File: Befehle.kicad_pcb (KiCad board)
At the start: 2 copper layers, 100 x 160 mm, 23 parts, among them P1 CONN_01X07, P2 CONN_01X07, U2 74LS540, U3 74LS541, U5 74LS373, U8 74LS139

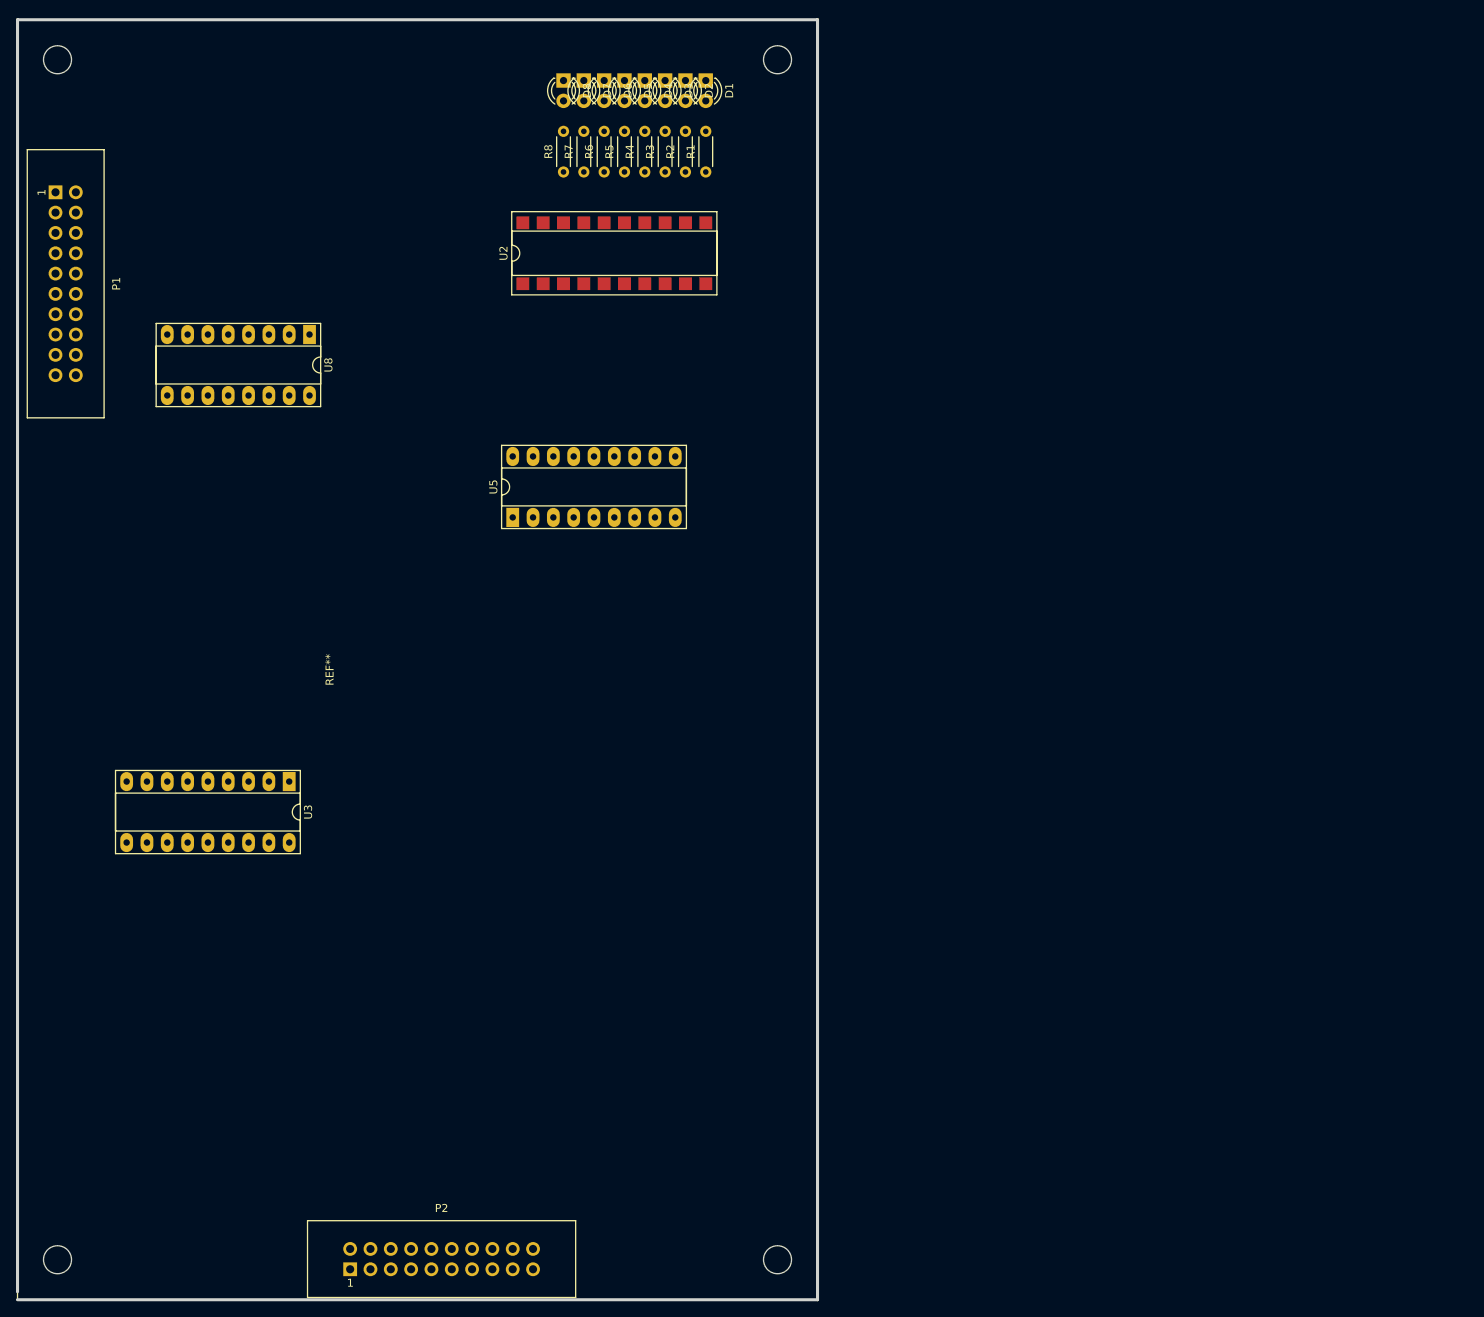
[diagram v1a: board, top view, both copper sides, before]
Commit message: Befehle Footprints und Leiterbahnen added
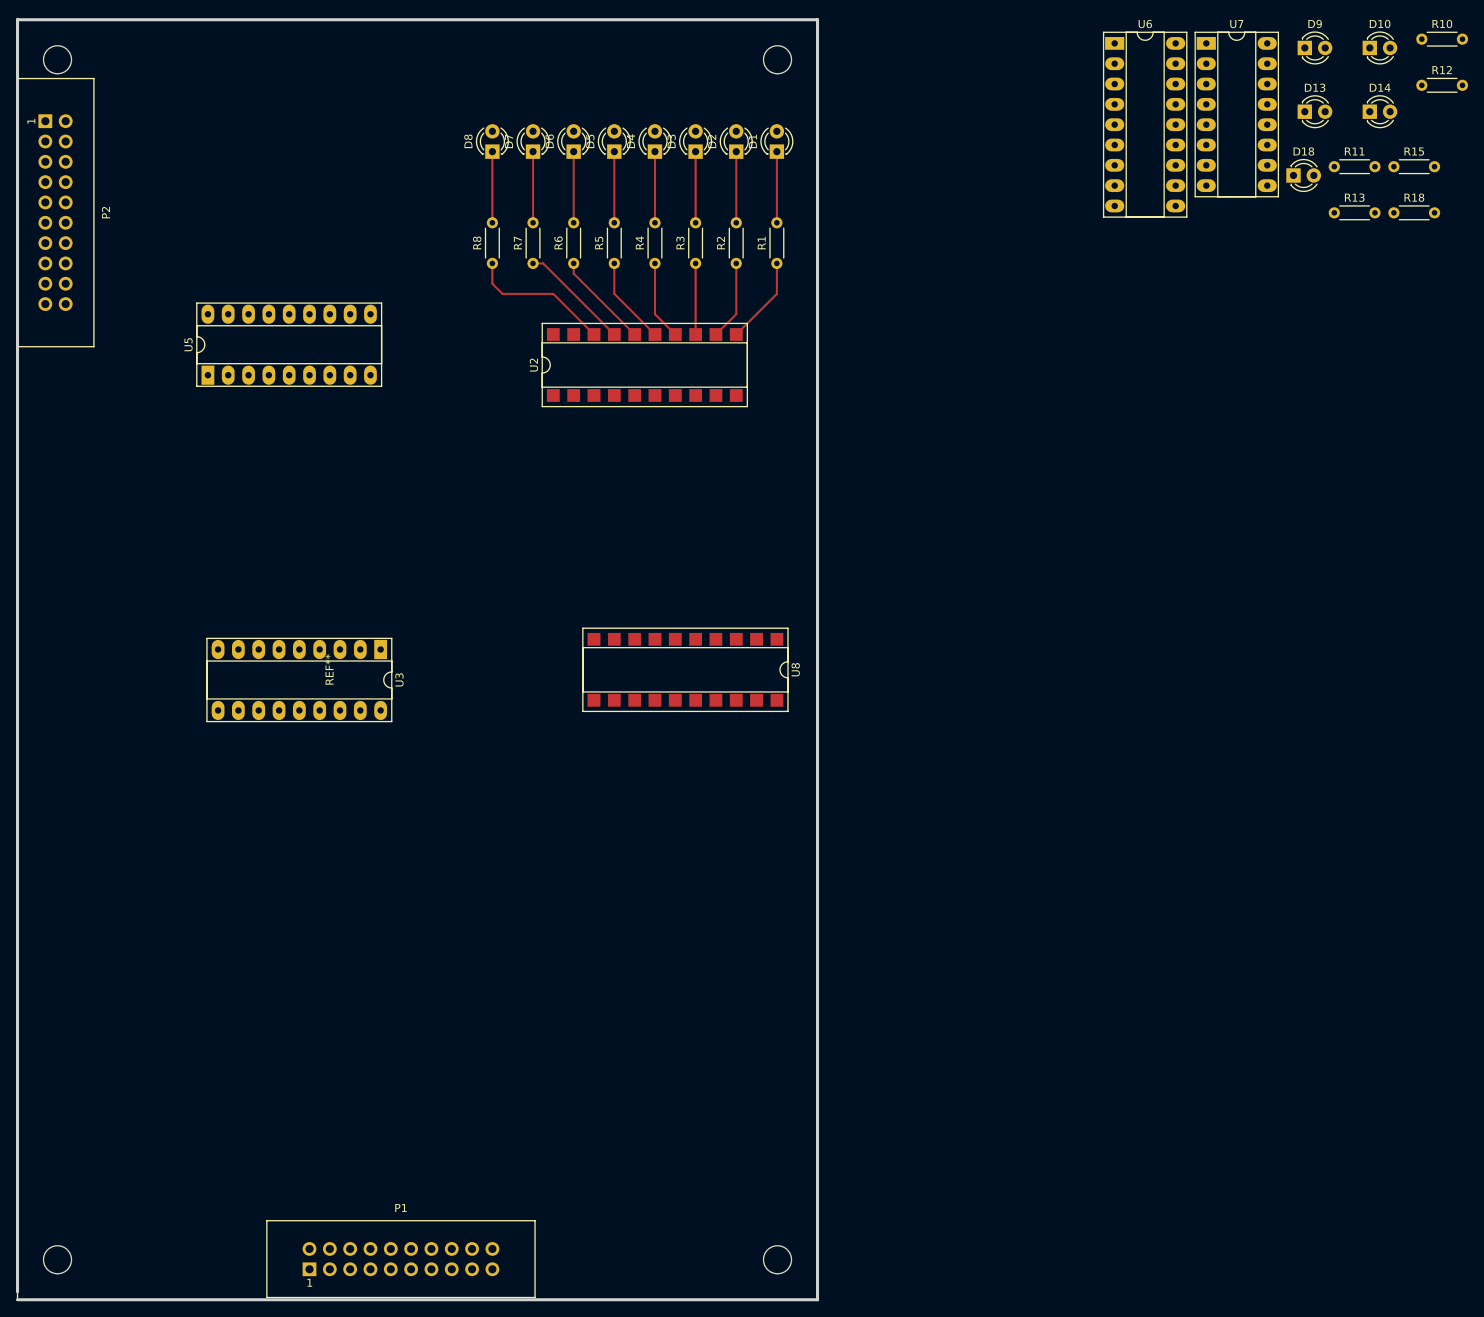
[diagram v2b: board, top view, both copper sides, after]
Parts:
- added D10: Led_Small, LEDs:LED_D3.0mm, F.Cu at (189.7, 21.3)
- added D13: Led_Small, LEDs:LED_D3.0mm, F.Cu at (181.6, 29.3)
- added D14: Led_Small, LEDs:LED_D3.0mm, F.Cu at (189.7, 29.3)
- added D18: LED, LEDs:LED_D3.0mm, F.Cu at (180.1, 37.3)
- added D9: Led_Small, LEDs:LED_D3.0mm, F.Cu at (181.6, 21.3)
- added R10: 330, Resistors_ThroughHole:R_Axial_DIN0204_L3.6mm_D1.6mm_P5.08mm_Horizontal, F.Cu at (196.2, 20.2)
- added R11: 330, Resistors_ThroughHole:R_Axial_DIN0204_L3.6mm_D1.6mm_P5.08mm_Horizontal, F.Cu at (185.2, 36.2)
- added R12: 330, Resistors_ThroughHole:R_Axial_DIN0204_L3.6mm_D1.6mm_P5.08mm_Horizontal, F.Cu at (196.2, 26.0)
- added R13: 330, Resistors_ThroughHole:R_Axial_DIN0204_L3.6mm_D1.6mm_P5.08mm_Horizontal, F.Cu at (185.2, 41.9)
- added R15: 330, Resistors_ThroughHole:R_Axial_DIN0204_L3.6mm_D1.6mm_P5.08mm_Horizontal, F.Cu at (192.7, 36.2)
- added R18: 330, Resistors_ThroughHole:R_Axial_DIN0204_L3.6mm_D1.6mm_P5.08mm_Horizontal, F.Cu at (192.7, 41.9)
- added U6: 74LS373, Housings_DIP:DIP-18_W7.62mm_Socket_LongPads, F.Cu at (157.8, 20.8)
- added U7: 74LS139, Housings_DIP:DIP-16_W7.62mm_Socket_LongPads, F.Cu at (169.2, 20.8)
- D3, D4, D7: value Led_Small -> LED
- P2: value CONN_01X07 -> CONN_02X10
- R1: value 330 -> 4,7k
- R4: value 330 -> 1k
- U2: value 74LS540 -> 74LS04
- U3: value 74LS541 -> 7400
- U5: value 74LS373 -> 74LS541
- U8: value 74LS139 -> 74LS540; footprint Housings_DIP:DIP-16_W7.62mm_Socket_LongPads -> Housings_DIP:DIP-20_W7.62mm_SMDSocket_SmallPads
- moved P2 148.5 mm to (24.1, 30.5), turned to 270 degrees
- moved P1 138.3 mm to (57.1, 174.0), turned to 0 degrees
- moved U8 63.0 mm to (104.1, 99.1)
- moved U5 42.0 mm to (44.5, 62.2)
- moved U3 20.1 mm to (66.0, 96.5)
- moved R8 14.5 mm to (80.0, 48.3)
- moved U2 14.5 mm to (99.1, 61.0)
- moved R1 14.5 mm to (115.6, 48.3)
- moved R2 13.1 mm to (110.5, 48.3)
- moved R7 13.1 mm to (85.1, 48.3)
- moved D8 12.6 mm to (80.0, 34.3), turned to 90 degrees
- moved D1 12.6 mm to (115.6, 34.3), turned to 90 degrees
- moved R3 12.0 mm to (105.4, 48.3)
- moved R6 12.0 mm to (90.2, 48.3)
- moved R4 11.5 mm to (100.3, 48.3)
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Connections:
- D1 pad 2: Net-(D1-Pad2) -> VCC
- D2 pad 2: Net-(D2-Pad2) -> VCC
- D4 pad 2: Net-(D4-Pad2) -> VCC
- D7 pad 2: Net-(D7-Pad2) -> VCC
- P2 pad 10: (no net) -> Net-(P2-Pad10)
- P2 pad 11: (no net) -> Net-(P2-Pad11)
- P2 pad 12: (no net) -> Net-(P2-Pad12)
- P2 pad 13: (no net) -> Net-(P2-Pad13)
- P2 pad 14: (no net) -> Net-(P2-Pad14)
- P2 pad 15: (no net) -> Net-(P2-Pad15)
- P2 pad 16: (no net) -> Net-(P2-Pad16)
- P2 pad 17: (no net) -> Net-(P2-Pad17)
- P2 pad 18: (no net) -> Net-(P2-Pad18)
- P2 pad 19: (no net) -> Net-(P2-Pad19)
- P2 pad 20: (no net) -> Net-(P2-Pad20)
- P2 pad 8: (no net) -> Net-(P2-Pad8)
- P2 pad 9: (no net) -> Net-(P2-Pad9)
- R1 pad 1: Net-(R1-Pad1) -> VCC
- R1 pad 2: Net-(D1-Pad1) -> enableR
- R2 pad 1: Net-(R2-Pad1) -> Net-(D1-Pad1)
- R2 pad 2: Net-(D2-Pad1) -> Net-(R2-Pad2)
- R3 pad 1: Net-(R3-Pad1) -> Net-(D2-Pad1)
- R3 pad 2: Net-(D3-Pad1) -> Net-(R3-Pad2)
- R4 pad 2: Net-(D4-Pad1) -> VCC
- R5 pad 2: Net-(D5-Pad1) -> Net-(R5-Pad2)
- R6 pad 1: Net-(R6-Pad1) -> Net-(D4-Pad1)
- R6 pad 2: Net-(D6-Pad1) -> Net-(R6-Pad2)
- R7 pad 2: Net-(D7-Pad1) -> Net-(D5-Pad1)
- R8 pad 2: Net-(D8-Pad1) -> Net-(D6-Pad1)
- U2 pad 1: Net-(U2-Pad1) -> Net-(R4-Pad1)
- U2 pad 10: GND -> Net-(R17-Pad2)
- U2 pad 11: Net-(R1-Pad1) -> 1
- U2 pad 12: Net-(R2-Pad1) -> Net-(R21-Pad2)
- U2 pad 13: Net-(R3-Pad1) -> 0
- U2 pad 14: Net-(R4-Pad1) -> VCC
- U2 pad 15: Net-(R5-Pad1) -> (no net)
- U2 pad 16: Net-(R6-Pad1) -> (no net)
- U2 pad 17: Net-(R7-Pad1) -> (no net)
- U2 pad 18: Net-(R8-Pad1) -> (no net)
- U2 pad 19: Net-(U2-Pad1) -> (no net)
- U2 pad 2: /a8 -> Net-(R2-Pad2)
- U2 pad 20: VCC -> (no net)
- U2 pad 3: /a7 -> loadIR
- U2 pad 4: /a6 -> Net-(R5-Pad2)
- U2 pad 5: /a5 -> 3
- U2 pad 6: /a4 -> Net-(R6-Pad2)
- U2 pad 7: /a3 -> GND
- U2 pad 8: /a2 -> Net-(R9-Pad2)
- U2 pad 9: /a1 -> 2
- U3 pad 1: Net-(U1-Pad2) -> incPCz
- U3 pad 10: GND -> Net-(U3-Pad10)
- U3 pad 11: Net-(U3-Pad11) -> upPC
- U3 pad 13: Net-(U3-Pad13) -> Net-(U3-Pad12)
- U3 pad 14: Net-(U3-Pad14) -> VCC
- U3 pad 15: Net-(U3-Pad15) -> (no net)
- U3 pad 16: Net-(U3-Pad16) -> (no net)
- U3 pad 17: Net-(U3-Pad17) -> (no net)
- U3 pad 18: Net-(U3-Pad11) -> (no net)
- U3 pad 2: /a8 -> incPCz
- U3 pad 3: /a7 -> Net-(U3-Pad3)
- U3 pad 4: /a6 -> Net-(R4-Pad1)
- U3 pad 5: /a5 -> Net-(U3-Pad3)
- U3 pad 6: /a4 -> Net-(U3-Pad10)
- U3 pad 7: /a3 -> GND
- U3 pad 8: GND -> Net-(U3-Pad8)
- U3 pad 9: GND -> incPC
- U5 pad 1: VCC -> Net-(U1-Pad6)
- U5 pad 11: Net-(R11-Pad2) -> Net-(P2-Pad3)
- U5 pad 12: /a4 -> Net-(P2-Pad5)
- U5 pad 13: Net-(U5-Pad13) -> Net-(P2-Pad7)
- U5 pad 14: Net-(U5-Pad14) -> Net-(P2-Pad9)
- U5 pad 15: /a3 -> Net-(P2-Pad11)
- U5 pad 16: Net-(U5-Pad16) -> Net-(P2-Pad13)
- U5 pad 17: Net-(U5-Pad17) -> Net-(P2-Pad15)
- U5 pad 18: Net-(U5-Pad18) -> Net-(P2-Pad17)
- U5 pad 3: Net-(U5-Pad3) -> /a7
- U5 pad 4: Net-(U5-Pad4) -> /a6
- U5 pad 5: /a7 -> /a5
- U5 pad 6: /a6 -> /a4
- U5 pad 7: Net-(U5-Pad7) -> /a3
- U5 pad 8: Net-(U5-Pad8) -> GND
- U5 pad 9: /a5 -> GND
- U8 pad 1: GND -> Net-(U8-Pad1)
- U8 pad 10: (no net) -> GND
- U8 pad 11: (no net) -> Net-(R18-Pad1)
- U8 pad 12: (no net) -> Net-(R15-Pad1)
- U8 pad 13: (no net) -> Net-(R13-Pad1)
- U8 pad 14: (no net) -> Net-(R12-Pad1)
- U8 pad 15: (no net) -> Net-(R11-Pad1)
- U8 pad 16: VCC -> Net-(R10-Pad1)
- U8 pad 2: Net-(U5-Pad19) -> /a8
- U8 pad 3: Net-(U5-Pad16) -> /a7
- U8 pad 4: Net-(U8-Pad4) -> /a6
- U8 pad 5: Net-(U8-Pad5) -> /a5
- U8 pad 6: Net-(U8-Pad6) -> /a4
- U8 pad 7: Net-(U8-Pad7) -> /a3
- U8 pad 8: GND -> /a2
- U8 pad 9: (no net) -> /a1
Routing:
- net Net-(D4-Pad1): track 0.00 -> 20.9 mm
- net Net-(R8-Pad1): track 0.00 -> 17.9 mm
- net Net-(D2-Pad1): track 0.00 -> 17.8 mm
- net Net-(D1-Pad1): track 0.00 -> 15.2 mm
- net Net-(R7-Pad1): track 0.00 -> 13.8 mm
- net Net-(R5-Pad1): track 0.00 -> 11.0 mm
- net Net-(D8-Pad1): track 0.00 -> 8.89 mm
- net Net-(D7-Pad1): track 0.00 -> 8.89 mm
- net Net-(D6-Pad1): track 0.00 -> 8.89 mm
- net Net-(D5-Pad1): track 0.00 -> 8.89 mm
- net Net-(D3-Pad1): track 0.00 -> 8.89 mm
- net VCC: track 0.00 -> 7.40 mm
- net 1: track 0.00 -> 7.18 mm
- net Net-(R4-Pad1): track 0.00 -> 6.35 mm
- net Net-(R21-Pad2): track 0.00 -> 3.59 mm

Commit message: bauteile angeordnet
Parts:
- moved D18 176.2 mm to (29.2, 128.3)
- moved R18 172.7 mm to (43.2, 128.3)
- moved D10 165.8 mm to (102.9, 162.6)
- moved D9 165.5 mm to (95.2, 162.6)
- moved D13 163.0 mm to (87.6, 162.6)
- moved R12 156.4 mm to (104.1, 152.4), turned to 90 degrees
- moved D14 155.0 mm to (110.5, 162.6)
- moved R13 142.8 mm to (88.9, 147.3), turned to 270 degrees
- moved R11 142.2 mm to (96.5, 147.3), turned to 270 degrees
- moved R15 137.5 mm to (111.8, 147.3), turned to 270 degrees
- moved U3 136.5 mm to (201.9, 109.2)
- moved U6 126.5 mm to (58.4, 99.1), turned to 90 degrees
- moved U7 105.3 mm to (151.1, 124.5)
- moved R10 72.3 mm to (144.8, 71.1), turned to 90 degrees
- moved U8 28.8 mm to (82.5, 118.1), turned to 0 degrees
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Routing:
- net 1: track 7.18 -> 4.58 mm
- net Net-(R21-Pad2): track 3.59 -> 1.27 mm
- net VCC: track 7.40 -> 9.05 mm
- net Net-(R8-Pad1): track 17.9 -> 19.2 mm
- net Net-(R5-Pad1): track 11.0 -> 12.3 mm
- net Net-(D4-Pad1): track 20.9 -> 22.1 mm
- net Net-(R7-Pad1): track 13.8 -> 15.0 mm
- net Net-(D2-Pad1): track 17.8 -> 16.9 mm

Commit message: pcb
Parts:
- moved U3 165.1 mm to (45.7, 162.6), turned to 180 degrees
- moved U8 71.7 mm to (148.6, 90.2)
- moved R10 62.3 mm to (82.5, 73.7)
- moved U7 54.0 mm to (110.5, 88.9), turned to 270 degrees
- moved U2 8.98 mm to (100.3, 68.6)
- moved U6 2.54 mm to (58.4, 96.5)
- moved R4 1.27 mm to (100.3, 47.0)
- moved R5 1.27 mm to (95.2, 47.0)
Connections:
- U3 pad 8: Net-(U3-Pad8) -> Net-(U3-Pad12)
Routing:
- net Net-(P2-Pad3): track 0.00 -> 74.1 mm
- net Net-(P2-Pad5): track 0.00 -> 69.7 mm
- net Net-(P2-Pad7): track 0.00 -> 65.4 mm
- net Net-(P2-Pad9): track 0.00 -> 61.1 mm
- net Net-(P2-Pad11): track 0.00 -> 56.7 mm
- net Net-(P2-Pad13): track 0.00 -> 52.4 mm
- net Net-(P2-Pad15): track 0.00 -> 48.0 mm
- net Net-(P2-Pad17): track 0.00 -> 43.7 mm
- net Net-(R21-Pad2): track 1.27 -> 10.2 mm
- net 1: track 4.58 -> 13.3 mm
- net Net-(D2-Pad1): track 16.9 -> 25.4 mm
- net Net-(R5-Pad1): track 12.3 -> 19.3 mm
- net Net-(R8-Pad1): track 19.2 -> 24.9 mm
- net Net-(R7-Pad1): track 15.0 -> 20.7 mm
- net VCC: track 9.05 -> 14.7 mm
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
